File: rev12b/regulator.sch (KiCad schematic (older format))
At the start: 21 parts, among them IC1 PIC12F675-I/P, Q1 PN2222A, Q2 2N2907A, Q3 BUK9511-55A (Logic Level), Q4 PN2222A, U1 LM7805

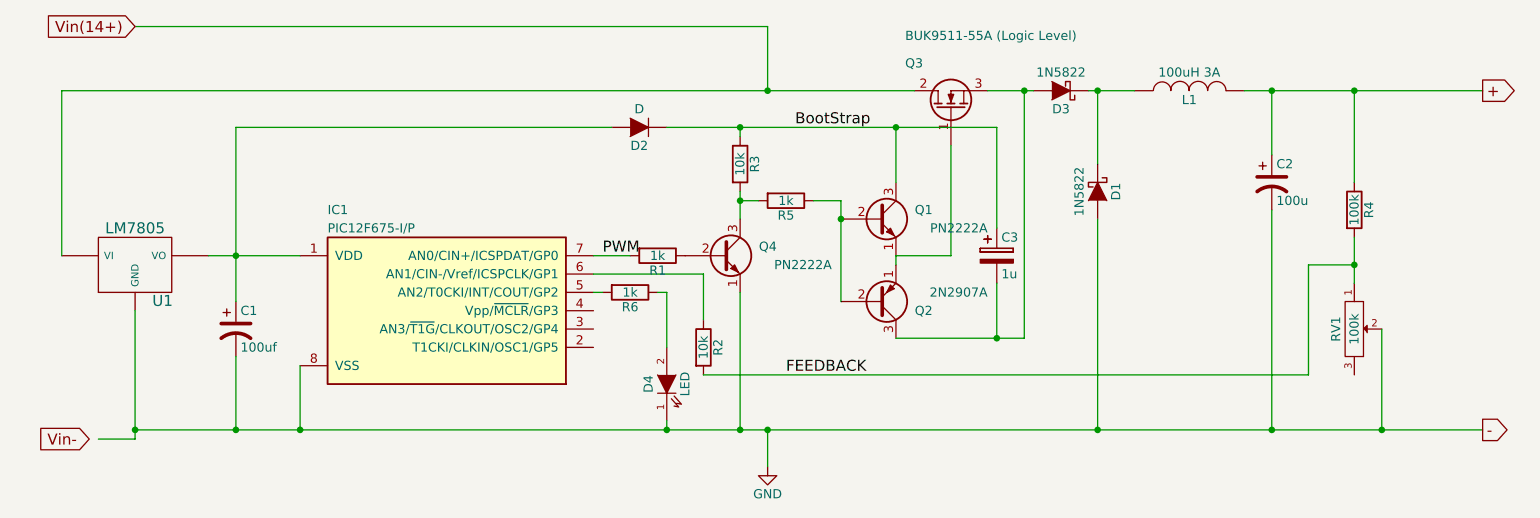
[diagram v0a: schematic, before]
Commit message: Update diode value.
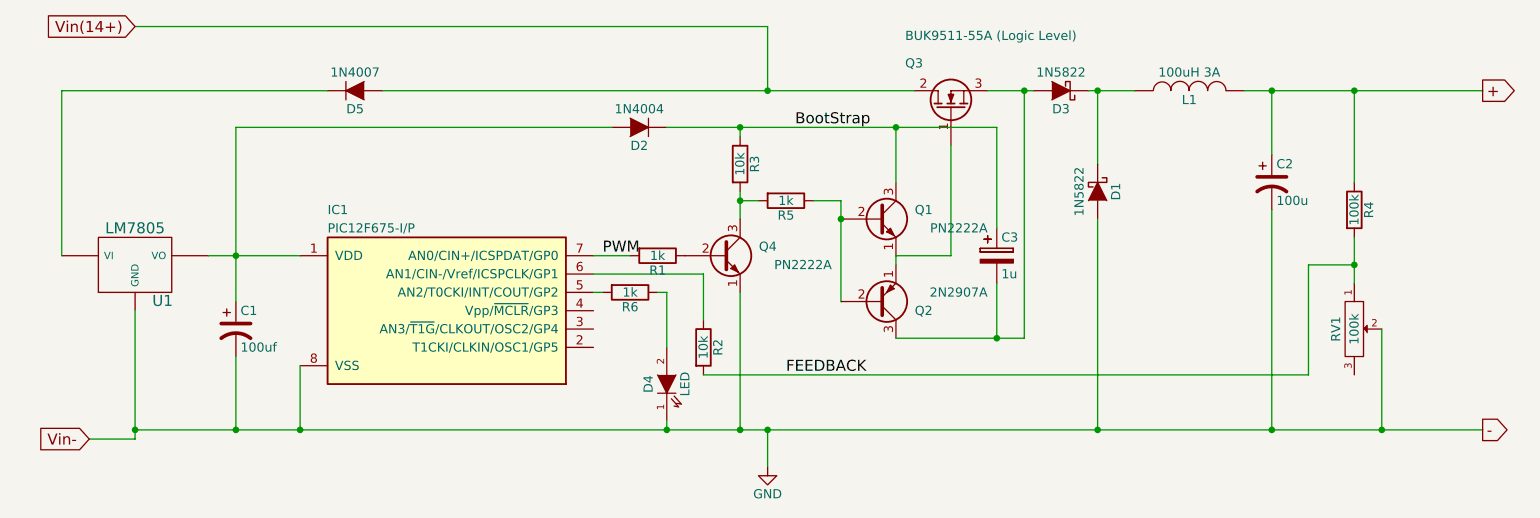
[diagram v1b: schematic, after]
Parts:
- added D5: 1N4007, symbol D
- D2: value D -> 1N4004
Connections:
- net Vin(14+): now also D5.2 (A); no longer U1.VI
- new net: D5.1 (K), U1.VI
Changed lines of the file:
@@
 Title "PWM Regulator v2"
 Date "2015-06-18"
-Rev "1.2b"
+Rev "1.2c"
 Comp ""
 Comment1 ""
@@
 P 4900 3350
 F 0 "D2" H 4900 3450 50  0000 C CNN
-F 1 "D" H 4900 3250 50  0000 C CNN
+F 1 "1N4004" H 4900 3250 50  0000 C CNN
 F 2 "" H 4900 3350 60  0000 C CNN
 F 3 "" H 4900 3350 60  0000 C CNN
@@
 Connection ~ 5450 3750
 Wire Wire Line
-	5450 4250 5450 5000
+	5450 5000 5450 4250
 Connection ~ 5450 5000
 Wire Wire Line
@@
 $EndComp
 Wire Wire Line
-	7600 3150 7350 3150
-Wire Wire Line
-	7050 3150 6800 3150
+	7350 3150 7600 3150
+Wire Wire Line
+	6800 3150 7050 3150
 Wire Wire Line
 	1750 3150 1750 4050
@@
 Vin-
 Wire Wire Line
-	2150 5050 1950 5050
+	2150 5050 1900 5050
 Connection ~ 2150 5000
 $Comp
@@
 	2700 3350 4750 3350
 Wire Wire Line
-	1750 3150 6400 3150
+	3500 3150 6400 3150
+$Comp
+L D D5
+U 1 1 558499A4
+P 3350 3150
+F 0 "D5" H 3350 3250 50  0000 C CNN
+F 1 "1N4007" H 3350 3050 50  0000 C CNN
+F 2 "" H 3350 3150 60  0000 C CNN
+F 3 "" H 3350 3150 60  0000 C CNN
+	1    3350 3150
+	1    0    0    1
+$EndComp
+Wire Wire Line
+	3200 3150 1750 3150
 $EndSCHEMATC
